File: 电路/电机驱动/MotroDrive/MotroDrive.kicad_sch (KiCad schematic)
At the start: 19 parts, among them J1 Conn_01x04_MountingPin, J2 Conn_01x02_MountingPin, U1 TLV61048DBVR

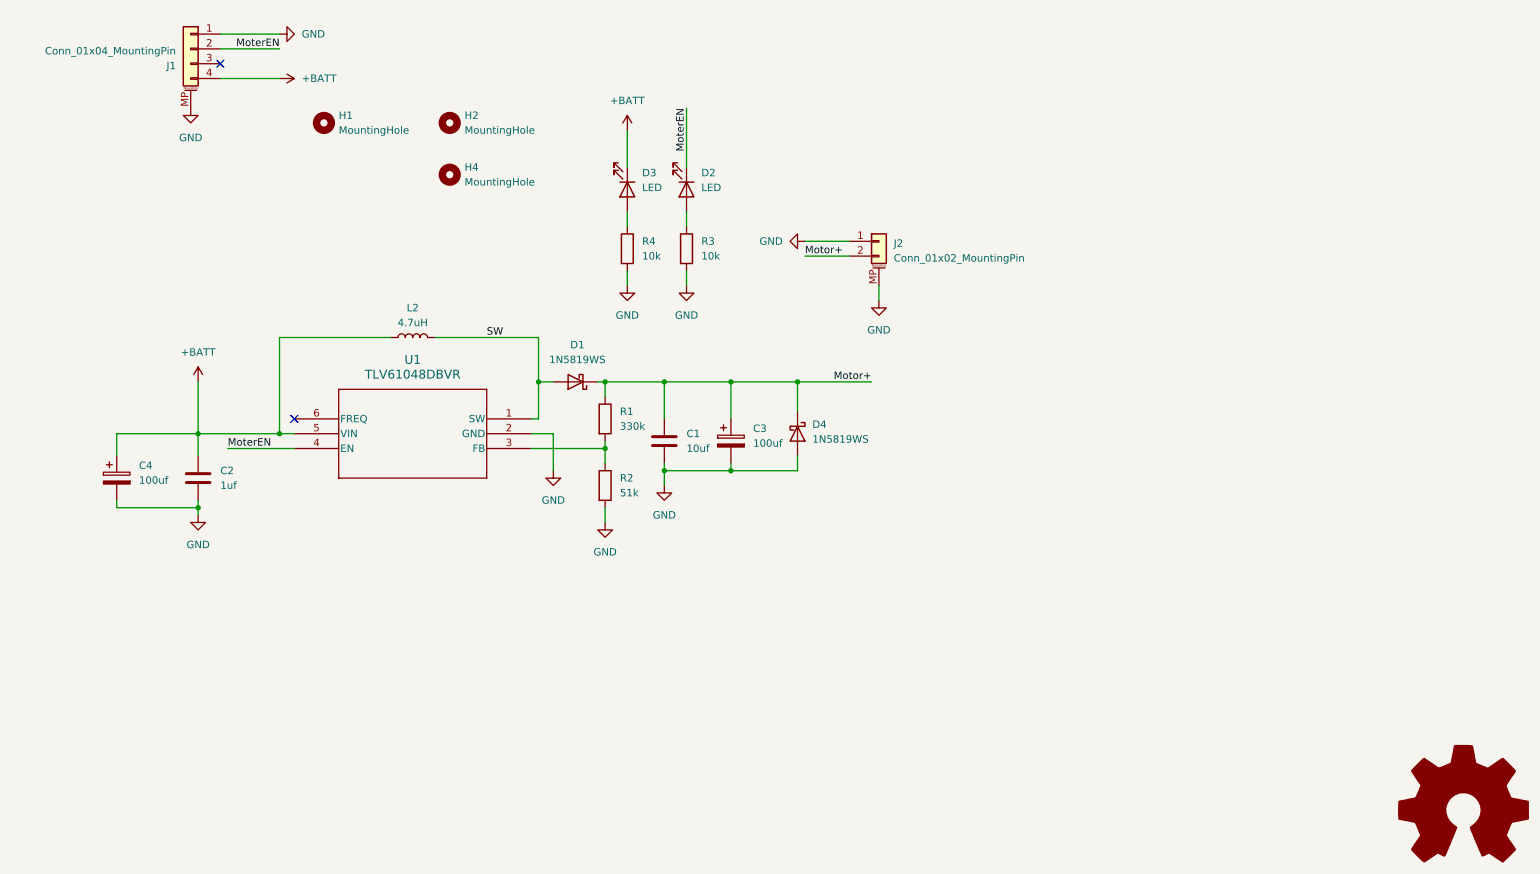
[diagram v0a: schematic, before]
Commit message: 主控升级至Rev1.2，电机驱动 Rev1.1
电机驱动修改后采用Mosfet控制高侧电源通路。主控配套进行了更改。
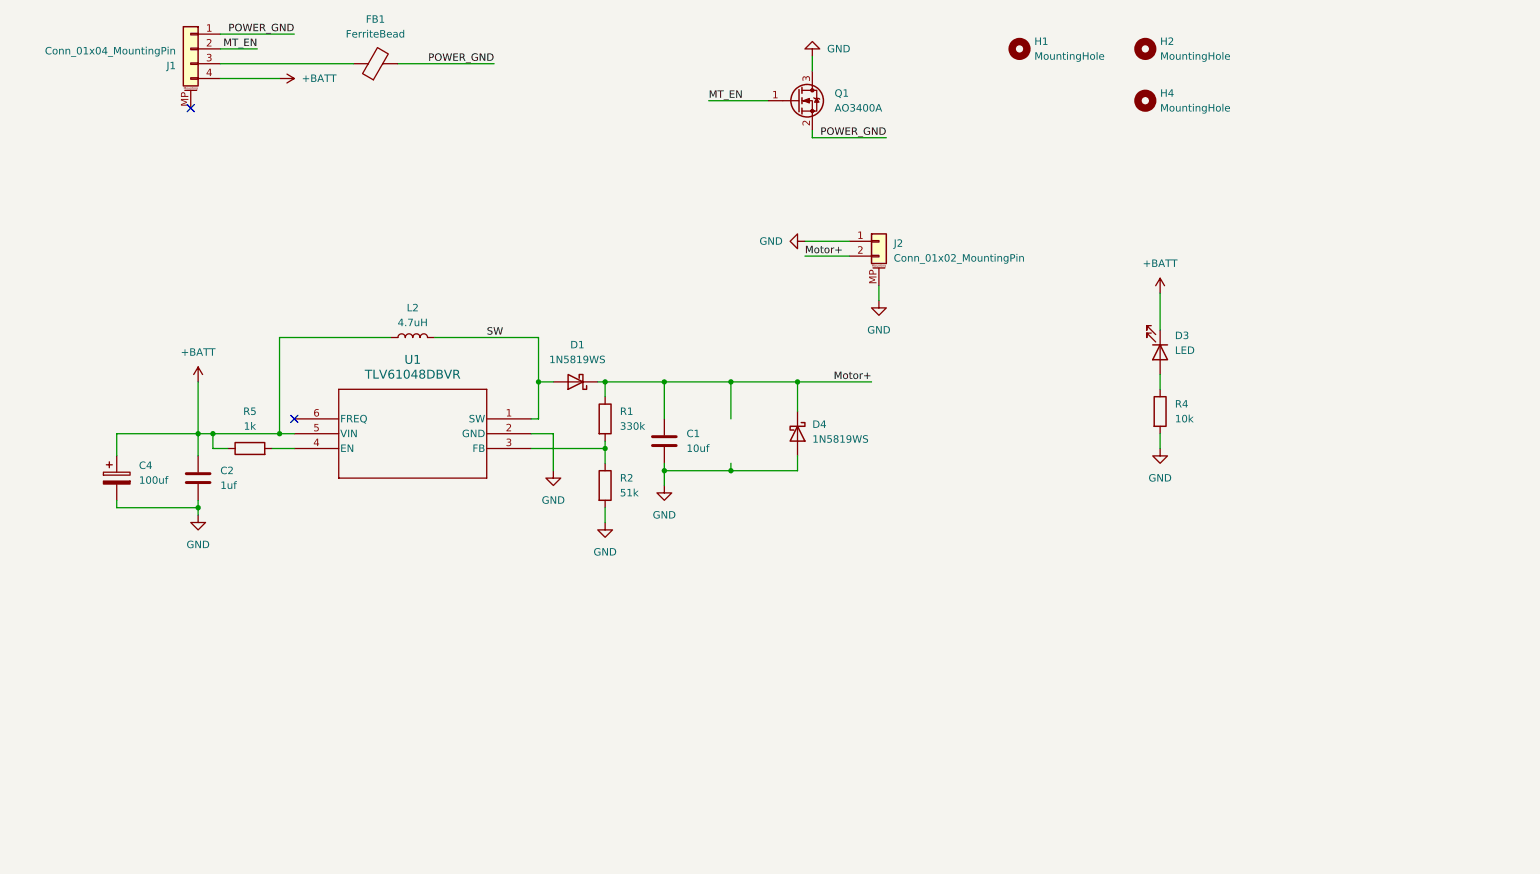
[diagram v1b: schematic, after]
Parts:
- removed C3: 100uf, Capacitor_SMD:CP_Elec_6.3x7.7, symbol Device:C_Polarized
- removed D2: LED, LED_SMD:LED_0805_2012Metric_Pad1.15x1.40mm_HandSolder, symbol Device:LED
- removed R3: 10k, Resistor_SMD:R_0603_1608Metric_Pad0.98x0.95mm_HandSolder, symbol Device:R
- added FB1: FerriteBead, Inductor_SMD:L_0603_1608Metric, symbol Device:FerriteBead
- added Q1: AO3400A, Package_TO_SOT_SMD:SOT-23, symbol Transistor_FET:AO3400A
- added R5: 1k, Resistor_SMD:R_0603_1608Metric, symbol Device:R
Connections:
- net +BATT: now also R5.1
- net GND: now also Q1.3 (D); no longer J1.1 (Pin_1), J1.MP (MountPin)
- net at J1.3 (Pin_3): now also FB1.1
- net MoterEN: no longer names the net of U1.4 (EN)
- net MoterEN: now also R5.2; no longer J1.2 (Pin_2)
- new net MT_EN: J1.2 (Pin_2), Q1.1 (G)
- new net POWER_GND: FB1.2, J1.1 (Pin_1), Q1.2 (S)
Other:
- moved on the sheet: D3, H1, H2, H4, R4

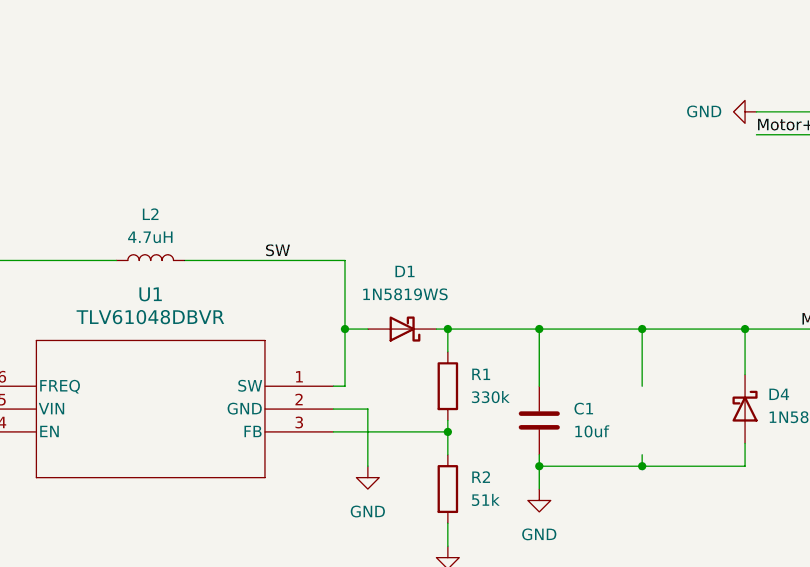
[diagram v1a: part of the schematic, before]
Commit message: 原本齿轮定位尺寸ok不应再加高度；修改电机驱动电路，但是电机驱动电路未完全ok
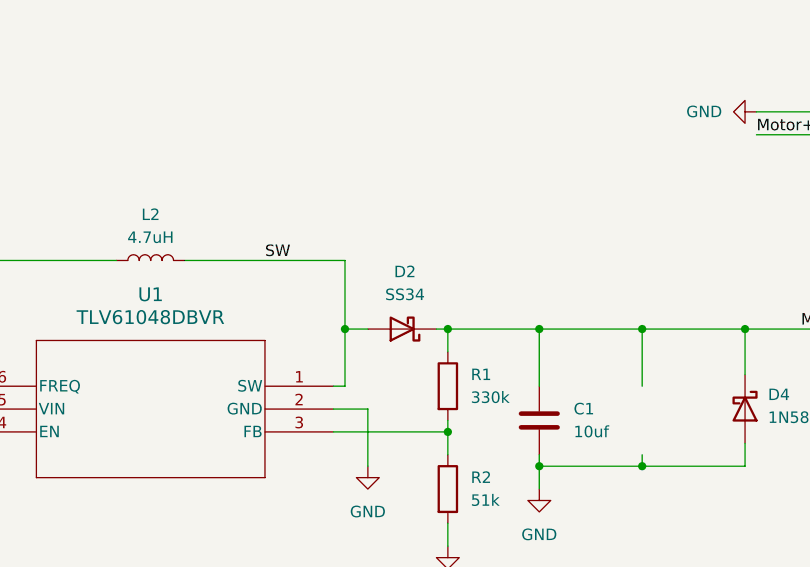
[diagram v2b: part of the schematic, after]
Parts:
- removed D1: 1N5819WS, Diode_SMD:D_SOD-323_HandSoldering, symbol Diode:1N5819WS
- added D2: SS34, Diode_SMD:D_SMA, symbol Diode:SS34
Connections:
- net Motor+: now also D2.1 (K)
- net SW: now also D2.2 (A)
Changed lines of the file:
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@@
-	)
-	(symbol
-		(lib_id "Diode:1N5819WS")
-		(at 107.95 78.74 180)
-		(unit 1)
-		(exclude_from_sim no)
-		(in_bom yes)
-		(on_board yes)
-		(dnp no)
-		(fields_autoplaced yes)
-		(property "Reference" "D1"
-			(at 108.2675 72.39 0)
-			(effects
-				(font
-					(size 1.27 1.27)
-				)
-			)
-		)
-		(property "Value" "1N5819WS"
-			(at 108.2675 74.93 0)
-			(effects
-				(font
-					(size 1.27 1.27)
-				)
-			)
-		)
-		(property "Footprint" "Diode_SMD:D_SOD-323_HandSoldering"
-			(at 107.95 74.295 0)
-			(effects
-				(font
-					(size 1.27 1.27)
-				)
-				(hide yes)
-			)
-		)
-		(property "Datasheet" "https://datasheet.lcsc.com/lcsc/2204281430_Guangdong-Hottech-1N5819WS_C191023.pdf"
-			(at 107.95 78.74 0)
-			(effects
-				(font
-					(size 1.27 1.27)
-				)
-				(hide yes)
-			)
-		)
-		(property "Description" "40V 600mV@1A 1A SOD-323 Schottky Barrier Diodes, SOD-323"
-			(at 107.95 78.74 0)
-			(effects
-				(font
-					(size 1.27 1.27)
-				)
-				(hide yes)
-			)
-		)
-		(pin "2"
-		)
-		(pin "1"
-		)
-		(instances
-			(project ""
-				(path "/791ff7e0-81a0-4288-9576-1071b96d7ac6"
-					(reference "D1")
-					(unit 1)
-				)
-			)
-		)
 	)
 	(symbol
@@
 					(unit 1)
 				)
+			)
+		)
+	)
+	(symbol
+		(lib_id "Diode:SS34")
+		(at 107.95 78.74 180)
+		(unit 1)
+		(exclude_from_sim no)
+		(in_bom yes)
+		(on_board yes)
+		(dnp no)
+		(fields_autoplaced yes)
+		(property "Reference" "D2"
+			(at 108.2675 72.39 0)
+			(effects
+				(font
+					(size 1.27 1.27)
+				)
+			)
+		)
+		(property "Value" "SS34"
+			(at 108.2675 74.93 0)
+			(effects
+				(font
+					(size 1.27 1.27)
+				)
+			)
+		)
+		(property "Footprint" "Diode_SMD:D_SMA"
+			(at 107.95 74.295 0)
+			(effects
+				(font
+					(size 1.27 1.27)
+				)
+				(hide yes)
+			)
+		)
+		(property "Datasheet" "https://www.vishay.com/docs/88751/ss32.pdf"
+			(at 107.95 78.74 0)
+			(effects
+				(font
+					(size 1.27 1.27)
+				)
+				(hide yes)
+			)
+		)
+		(property "Description" "40V 3A Schottky Diode, SMA"
+			(at 107.95 78.74 0)
+			(effects
+				(font
+					(size 1.27 1.27)
+				)
+				(hide yes)
+			)
+		)
+		(pin "1"
+		)
+		(pin "2"
+		)
+		(instances
+			(project ""
+				(path "/791ff7e0-81a0-4288-9576-1071b96d7ac6"
+					(reference "D2")
+					(unit 1)
+				)

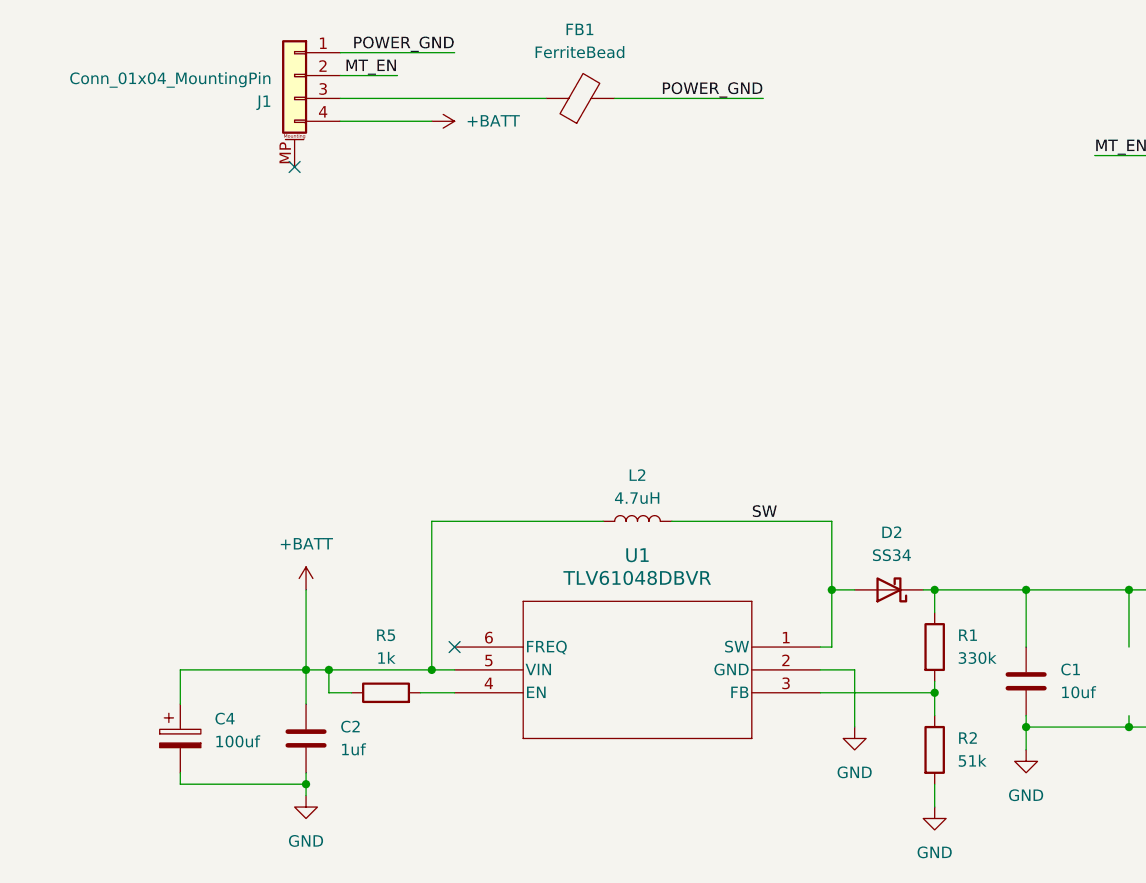
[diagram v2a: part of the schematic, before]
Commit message: 驱动电路升级至R1.2 未验证
R1.2 升压二极管改为SS34；储能电容改为连接原始电源GND；电路板改为单面布局
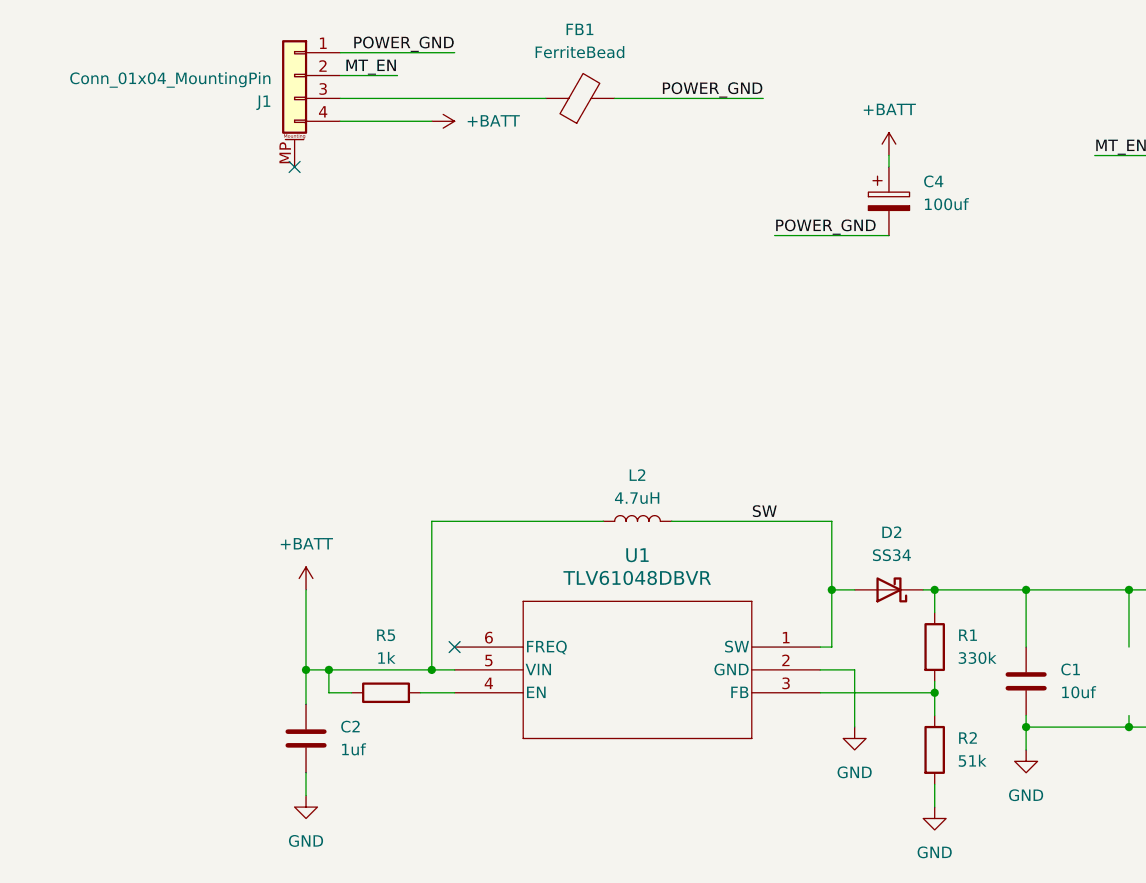
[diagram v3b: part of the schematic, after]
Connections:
- net GND: no longer C4.2
- net POWER_GND: now also C4.2
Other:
- moved on the sheet: C4
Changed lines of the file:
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@@
 	(paper "A4")
 	(title_block
-		(date "2026-01-21")
-		(rev "1.1")
-		(comment 1 "修改了上电逻辑")
+		(date "2026-03-15")
+		(rev "1.2")
+		(comment 1 "R1.1 修改了上电逻辑")
+		(comment 2 "R1.2 升压二极管改为SS34，修改为单面布局，输入储能电容改为电源GND")
 	)
 	(junction
@@
 		(color 0 0 0 0)
 	)
-	(junction
-		(at 43.18 100.33)
-		(diameter 0)
-		(color 0 0 0 0)
-	)
 	(no_connect
 		(at 41.91 31.75)
@@
 	(wire
 		(pts
-			(xy 43.18 100.33) (xy 43.18 101.6)
+			(xy 43.18 99.06) (xy 43.18 101.6)
+		)
+		(stroke
+			(width 0)
+			(type default)
+		)
+	)
+	(wire
+		(pts
+			(xy 95.25 39.37) (xy 107.95 39.37)
 		)
 		(stroke
@@
 	(wire
 		(pts
-			(xy 29.21 100.33) (xy 29.21 99.06)
-		)
-		(stroke
-			(width 0)
-			(type default)
-		)
-	)
-	(wire
-		(pts
 			(xy 57.15 87.63) (xy 59.69 87.63)
 		)
@@
 	(wire
 		(pts
-			(xy 29.21 100.33) (xy 43.18 100.33)
-		)
-		(stroke
-			(width 0)
-			(type default)
-		)
-	)
-	(wire
-		(pts
 			(xy 113.03 78.74) (xy 123.19 78.74)
 		)
@@
 	(wire
 		(pts
-			(xy 29.21 91.44) (xy 29.21 87.63)
-		)
-		(stroke
-			(width 0)
-			(type default)
-		)
-	)
-	(wire
-		(pts
 			(xy 160.02 62.23) (xy 160.02 64.77)
 		)
@@
 	(wire
 		(pts
-			(xy 43.18 99.06) (xy 43.18 100.33)
-		)
-		(stroke
-			(width 0)
-			(type default)
-		)
-	)
-	(wire
-		(pts
 			(xy 111.76 78.74) (xy 113.03 78.74)
 		)
@@
 	(wire
 		(pts
-			(xy 29.21 87.63) (xy 43.18 87.63)
-		)
-		(stroke
-			(width 0)
-			(type default)
-		)
-	)
-	(wire
-		(pts
 			(xy 43.18 91.44) (xy 43.18 87.63)
 		)
@@
 		(pts
 			(xy 134.62 92.71) (xy 134.62 93.98)
+		)
+		(stroke
+			(width 0)
+			(type default)
+		)
+	)
+	(wire
+		(pts
+			(xy 107.95 30.48) (xy 107.95 31.75)
 		)
 		(stroke
@@
 			)
 			(justify right bottom)
+		)
+	)
+	(label "POWER_GND"
+		(at 95.25 39.37 0)
+		(effects
+			(font
+				(size 1.27 1.27)
+			)
+			(justify left bottom)
 		)
 	)
@@
 	(symbol
 		(lib_id "power:+BATT")
+		(at 107.95 30.48 0)
+		(mirror y)
+		(unit 1)
+		(exclude_from_sim no)
+		(in_bom yes)
+		(on_board yes)
+		(dnp no)
+		(fields_autoplaced yes)
+		(property "Reference" "#PWR010"
+			(at 107.95 34.29 0)
+			(effects
+				(font
+					(size 1.27 1.27)
+				)
+				(hide yes)
+			)
+		)
+		(property "Value" "+BATT"
+			(at 107.95 25.4 0)
+			(effects
+				(font
+					(size 1.27 1.27)
+				)
+			)
+		)
+		(property "Footprint" ""
+			(at 107.95 30.48 0)
+			(effects
+				(font
+					(size 1.27 1.27)
+				)
+				(hide yes)
+			)
+		)
+		(property "Datasheet" ""
+			(at 107.95 30.48 0)
+			(effects
+				(font
+					(size 1.27 1.27)
+				)
+				(hide yes)
+			)
+		)
+		(property "Description" "Power symbol creates a global label with name \"+BATT\""
+			(at 107.95 30.48 0)
+			(effects
+				(font
+					(size 1.27 1.27)
+				)
+				(hide yes)
+			)
+		)
+		(pin "1"
+		)
+		(instances
+			(project "MotroDrive"
+				(path "/791ff7e0-81a0-4288-9576-1071b96d7ac6"
+					(reference "#PWR010")
+					(unit 1)
+				)
+			)
+		)
+	)
+	(symbol
+		(lib_id "power:+BATT")
 		(at 57.15 26.67 270)
 		(mirror x)
@@
 	(symbol
 		(lib_id "Device:C_Polarized")
-		(at 29.21 95.25 0)
+		(at 107.95 35.56 0)
 		(unit 1)
 		(exclude_from_sim no)
@@
 		(fields_autoplaced yes)
 		(property "Reference" "C4"
-			(at 33.02 93.0909 0)
+			(at 111.76 33.4009 0)
 			(effects
 				(font
@@
 		)
 		(property "Value" "100uf"
-			(at 33.02 95.6309 0)
+			(at 111.76 35.9409 0)
 			(effects
 				(font
@@
 		)
 		(property "Footprint" "Capacitor_SMD:CP_Elec_6.3x7.7"
-			(at 30.1752 99.06 0)
+			(at 108.9152 39.37 0)
 			(effects
 				(font
@@
 		)
 		(property "Datasheet" "~"
-			(at 29.21 95.25 0)
+			(at 107.95 35.56 0)
 			(effects
 				(font
@@
 		)
 		(property "Description" "Polarized capacitor"
-			(at 29.21 95.25 0)
-			(effects
-				(font
+			(at 107.95 35.56 0)
+			(effects
+				(font
